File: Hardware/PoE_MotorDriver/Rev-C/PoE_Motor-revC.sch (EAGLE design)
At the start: 78 parts, among them IC2 ATMEGA32U4-MU, J6 10103594-0001LF, SW1 SPST_TACT-KMR2, U1 DRV8871, U2 DRV8871, U4 W5500, X1 DCMOTOR, X2 J1011FHY931147C, X5 DCMOTOR, Y4 8MHz

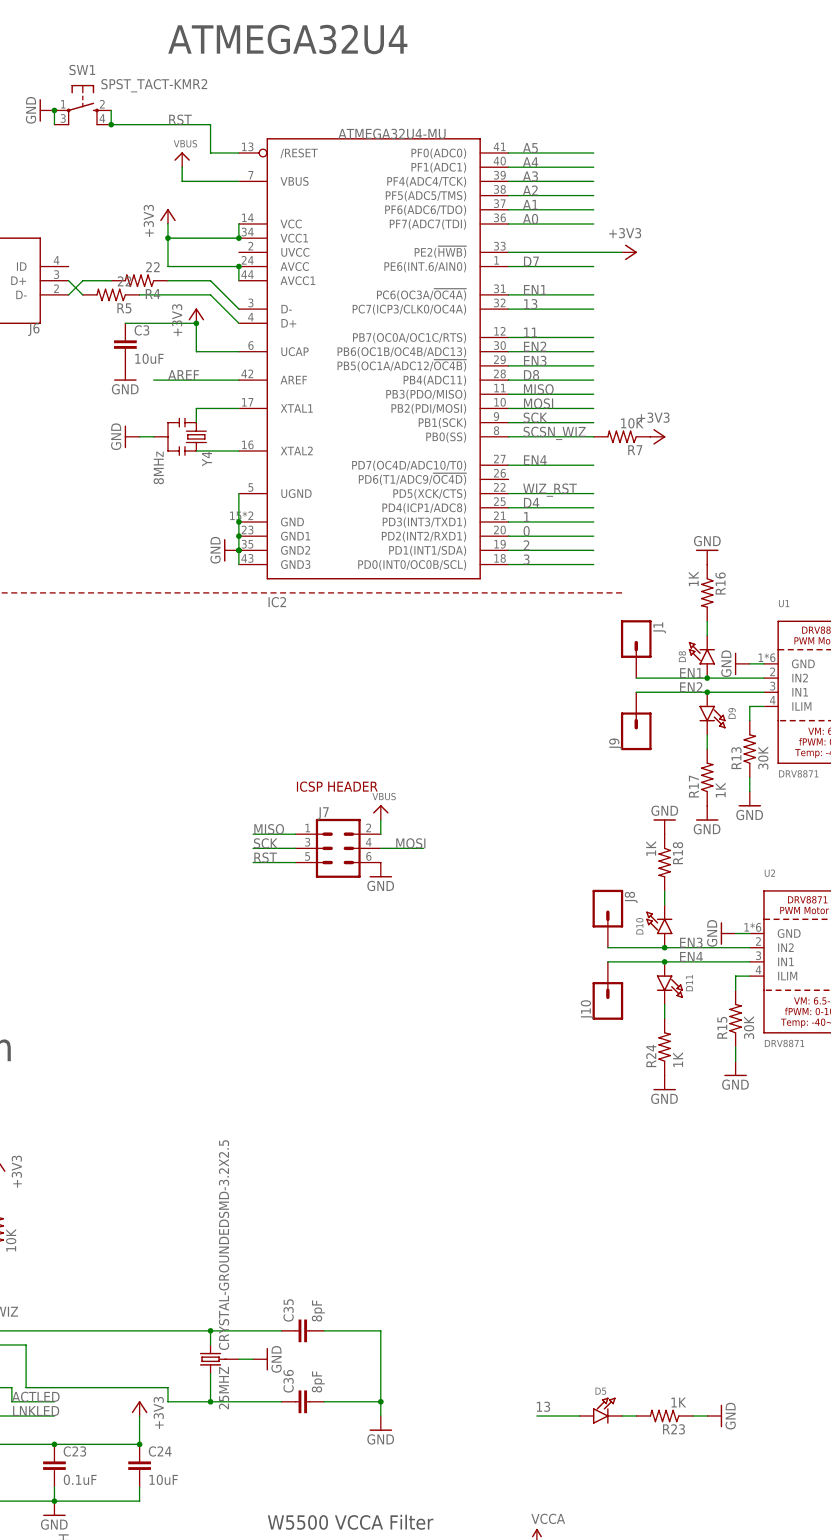
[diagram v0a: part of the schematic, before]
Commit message: HEEP-728 made values more readable on brd file
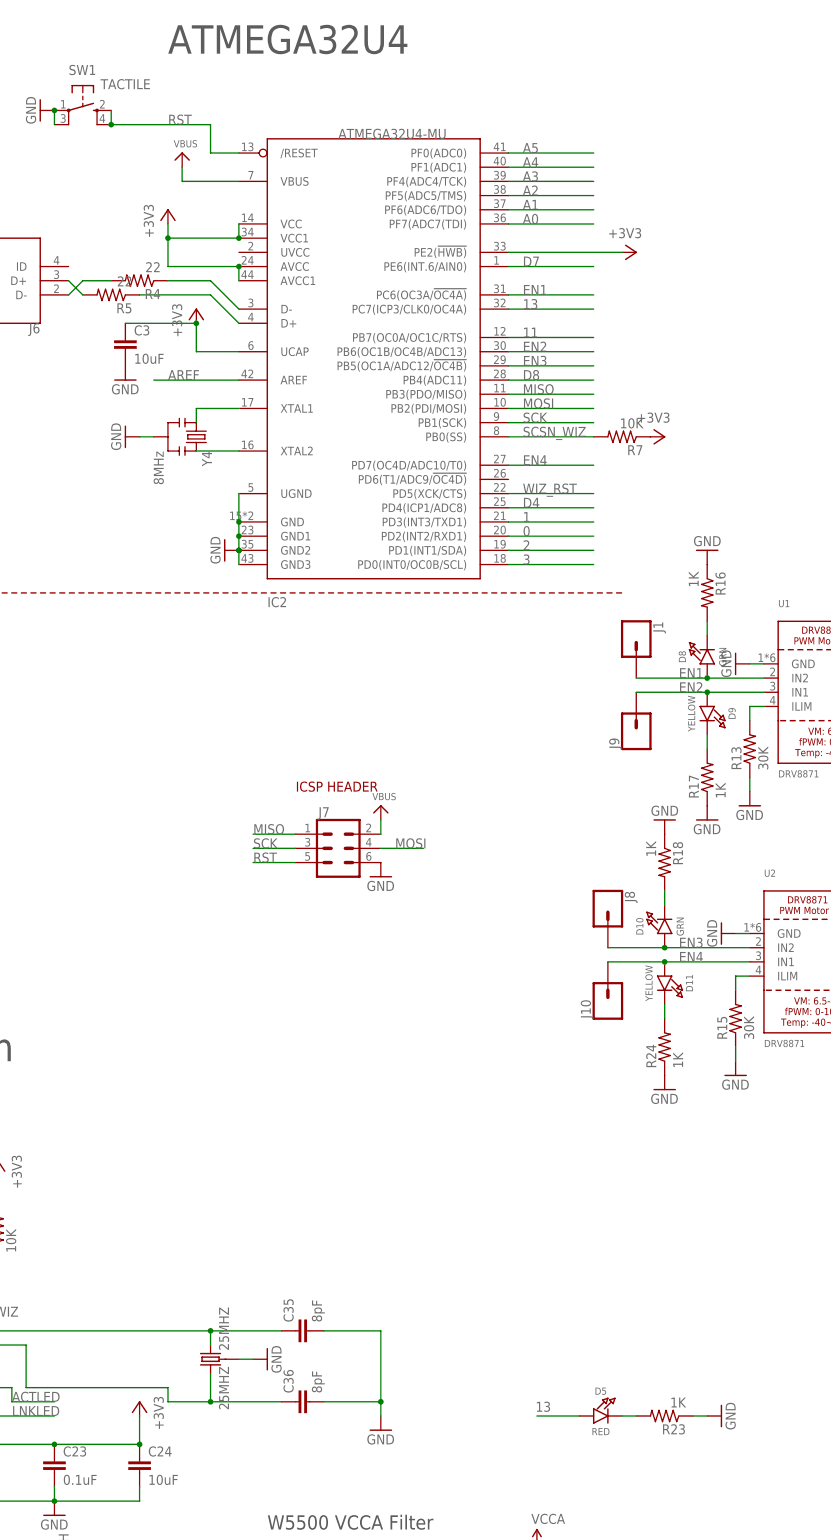
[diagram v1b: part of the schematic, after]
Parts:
- 25MHZ: value CRYSTAL-GROUNDEDSMD-3.2X2.5 -> 25MHZ
- D10, D8: value (none) -> GRN
- D11, D9: value (none) -> YELLOW
- D5: value (none) -> RED
- SW1: value SPST_TACT-KMR2 -> TACTILE
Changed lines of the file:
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@@
 <part name="GND30" library="SparkFun-Aesthetics" deviceset="GND" device=""/>
 <part name="GND33" library="SparkFun-Aesthetics" deviceset="GND" device=""/>
-<part name="25MHZ" library="SparkFun-Clocks" deviceset="CRYSTAL-GROUNDED" device="SMD-3.2X2.5"/>
+<part name="25MHZ" library="SparkFun-Clocks" deviceset="CRYSTAL-GROUNDED" device="SMD-3.2X2.5" value="25MHZ"/>
 <part name="GND36" library="SparkFun-Aesthetics" deviceset="GND" device=""/>
 <part name="C9" library="SparkFun-Passives" deviceset="CAP" device="0603-CAP" value="0.1uF"/>
@@
 <part name="U$5" library="microbuilder" deviceset="VBUS" device=""/>
 <part name="U$10" library="microbuilder" deviceset="VBUS" device=""/>
-<part name="SW1" library="adafruit" deviceset="SPST_TACT" device="-KMR2"/>
+<part name="SW1" library="adafruit" deviceset="SPST_TACT" device="-KMR2" value="TACTILE"/>
 <part name="GND34" library="supply1" deviceset="GND" device=""/>
 <part name="U$33" library="microbuilder" deviceset="VBAT" device=""/>
@@
 <part name="GND16" library="SparkFun-Aesthetics" deviceset="GND" device=""/>
 <part name="R23" library="SparkFun-Passives" deviceset="RESISTOR" device="0603-RES" value="1K"/>
-<part name="D5" library="microbuilder" deviceset="LED" device="0805_NOOUTLINE"/>
+<part name="D5" library="microbuilder" deviceset="LED" device="0805_NOOUTLINE" value="RED"/>
 <part name="GND17" library="SparkFun-Aesthetics" deviceset="GND" device=""/>
 <part name="+3V5" library="supply1" deviceset="+3V3" device=""/>
@@
 <part name="X5" library="microbuilder" deviceset="TERMBLOCK_1X2" device="" value="DCMOTOR"/>
 <part name="R16" library="SparkFun-Passives" deviceset="RESISTOR" device="0603-RES" value="1K"/>
-<part name="D8" library="microbuilder" deviceset="LED" device="0805_NOOUTLINE"/>
+<part name="D8" library="microbuilder" deviceset="LED" device="0805_NOOUTLINE" value="GRN"/>
 <part name="R17" library="SparkFun-Passives" deviceset="RESISTOR" device="0603-RES" value="1K"/>
-<part name="D9" library="microbuilder" deviceset="LED" device="0805_NOOUTLINE"/>
+<part name="D9" library="microbuilder" deviceset="LED" device="0805_NOOUTLINE" value="YELLOW"/>
 <part name="R18" library="SparkFun-Passives" deviceset="RESISTOR" device="0603-RES" value="1K"/>
-<part name="D10" library="microbuilder" deviceset="LED" device="0805_NOOUTLINE"/>
+<part name="D10" library="microbuilder" deviceset="LED" device="0805_NOOUTLINE" value="GRN"/>
 <part name="R24" library="SparkFun-Passives" deviceset="RESISTOR" device="0603-RES" value="1K"/>
-<part name="D11" library="microbuilder" deviceset="LED" device="0805_NOOUTLINE"/>
+<part name="D11" library="microbuilder" deviceset="LED" device="0805_NOOUTLINE" value="YELLOW"/>
 <part name="J1" library="SparkFun-Connectors" deviceset="CONN_01" device=""/>
 <part name="J8" library="SparkFun-Connectors" deviceset="CONN_01" device=""/>
